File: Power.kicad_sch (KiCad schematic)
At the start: 30 parts, among them J1 1769, U6 EA3036C, U9 BQ24074RGTR

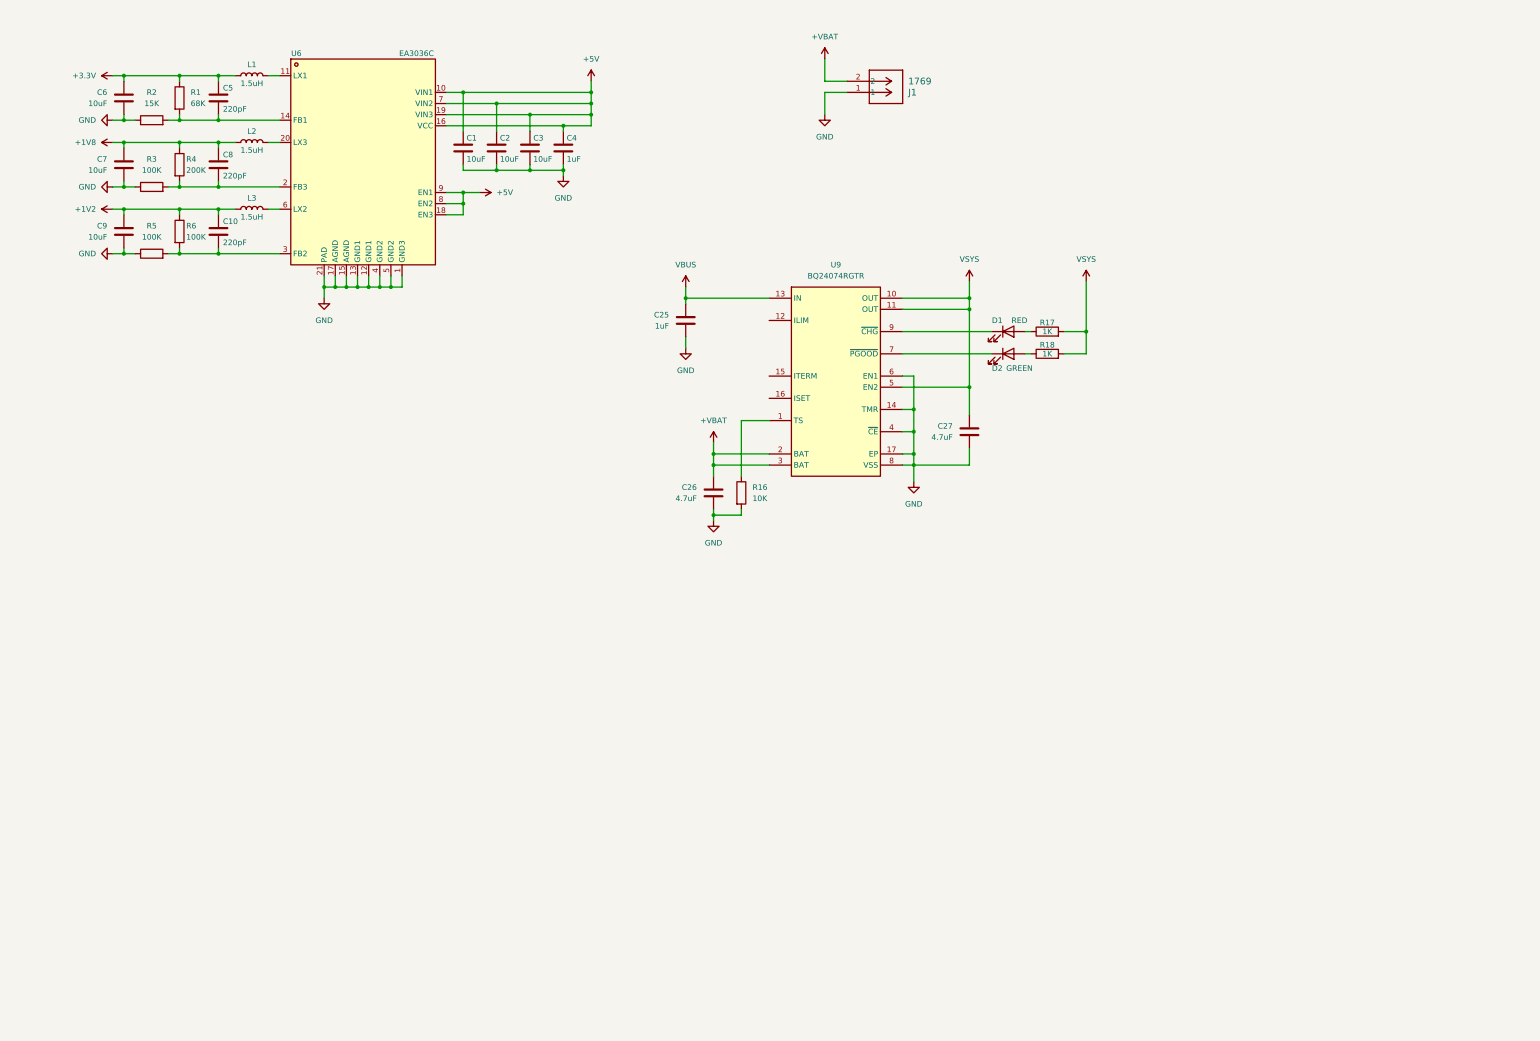
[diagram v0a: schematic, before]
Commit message: power changes, audio changes, testing layout
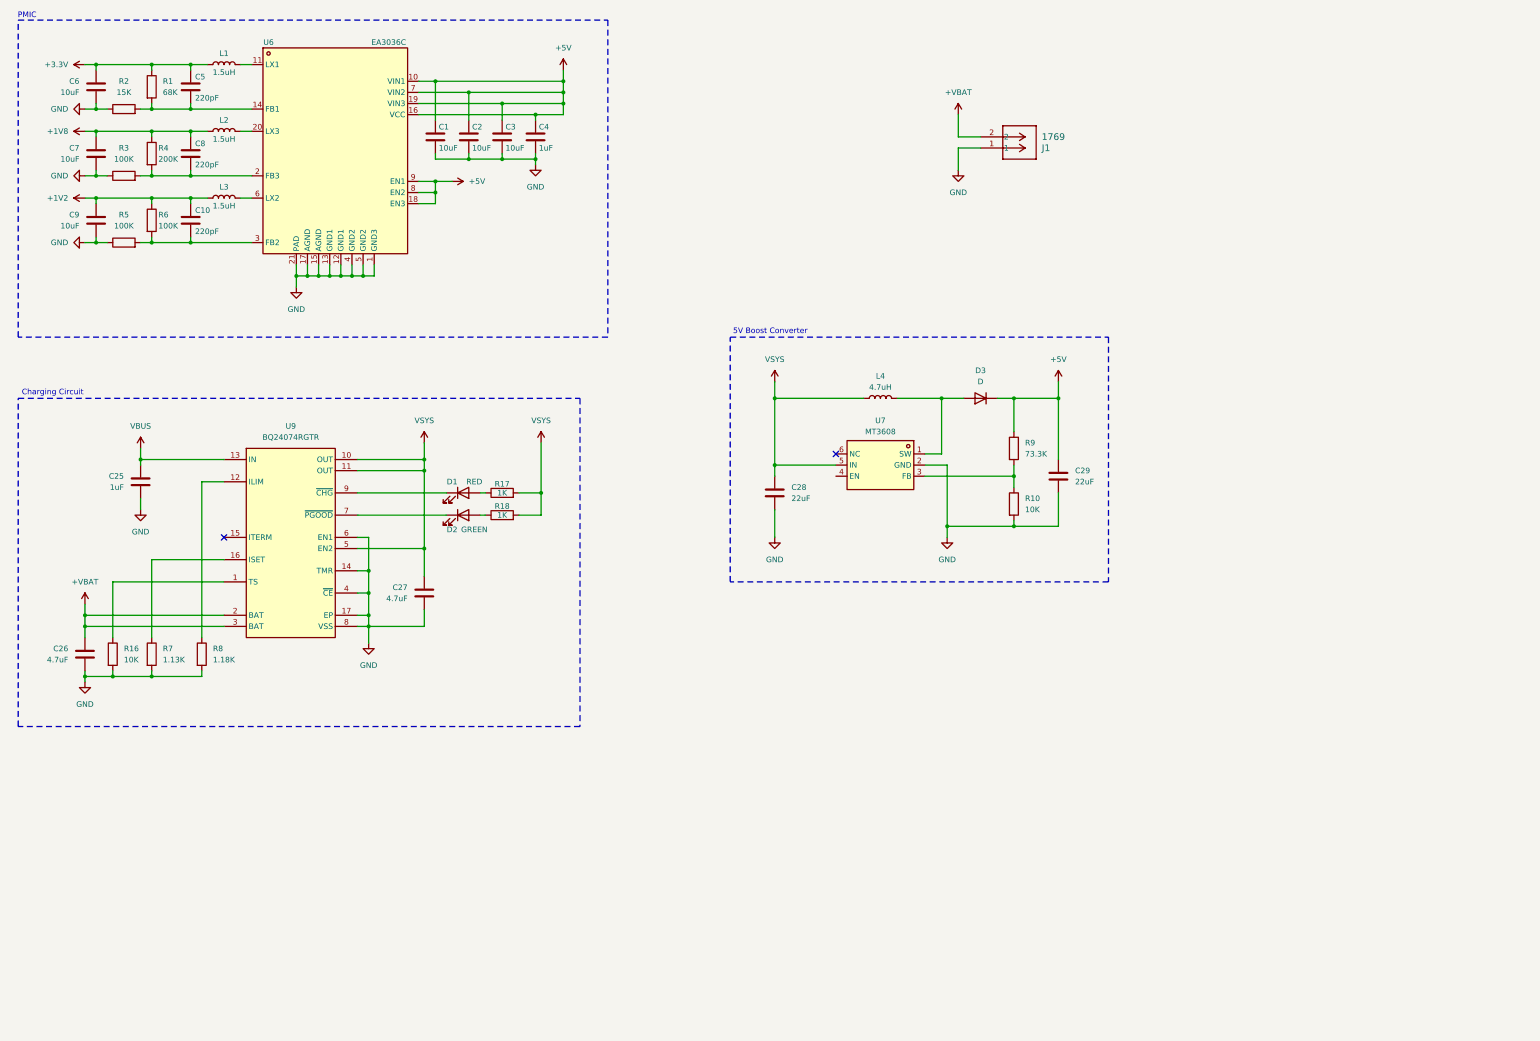
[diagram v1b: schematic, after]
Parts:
- added C28, C29: 22uF, symbol Device:C
- added D3: D, symbol Device:D
- added L4: 4.7uH, symbol Device:L
- added R10: 10K, symbol Device:R
- added R7: 1.13K, symbol Device:R
- added R8: 1.18K, symbol Device:R
- added R9: 73.3K, symbol Device:R
- added U7: MT3608, easyeda2kicad:SOT-23-6_L2.9-W1.6-P0.95-LS2.8-BL, symbol easyeda2kicad:MT3608
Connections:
- net +5V: now also C29.1, D3.1 (K), R9.1
- net GND: now also C28.2, C29.2, R10.2, R7.2, R8.2, U7.2 (GND)
- net VSYS: now also C28.1, L4.1, U7.5 (IN)
- net at U9.12 (ILIM): now also R8.1
- net at U9.16 (ISET): now also R7.1
- new net: D3.2 (A), L4.2, U7.1 (SW)
- new net: R10.1, R9.2, U7.3 (FB)
- no-connect marks 0 -> 2
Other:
- note added: "5V Boost Converter"
- note added: "Charging Circuit"
- note added: "PMIC"
- moved on the sheet: C1, C10, C2, C25, C26, C27, C3, C4, C5, C6, C7, C8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

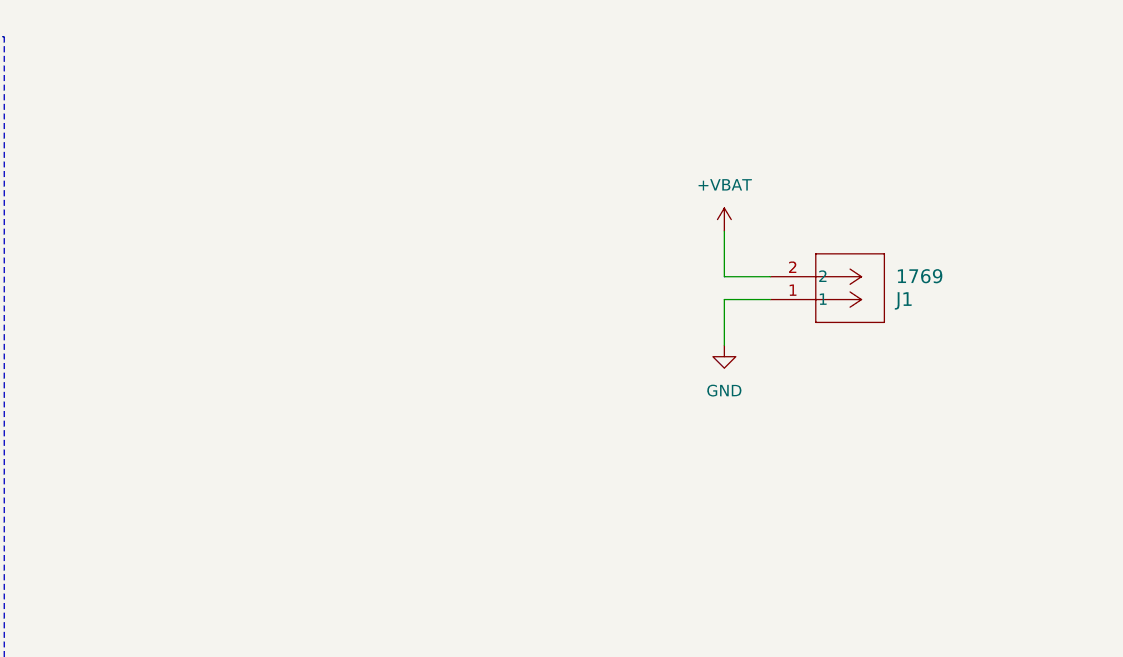
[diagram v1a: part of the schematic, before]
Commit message: power changes to v3s, nand
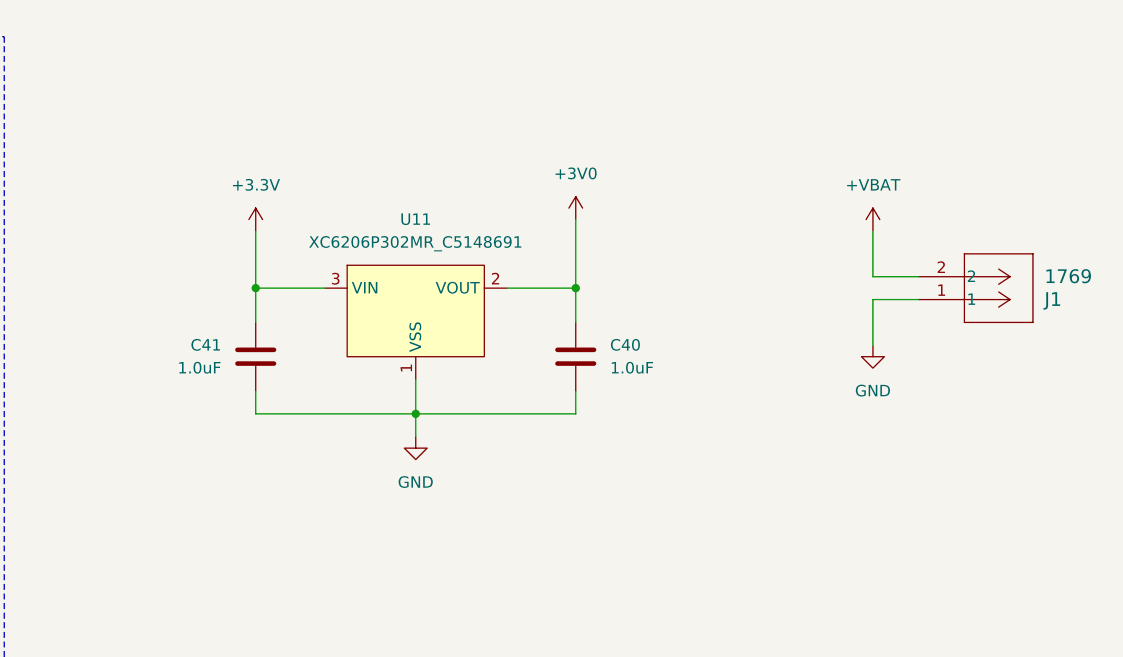
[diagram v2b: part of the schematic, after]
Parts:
- added C40, C41: 1.0uF, symbol Device:C
- added U11: XC6206P302MR_C5148691, easyeda2kicad:SOT-23-3_L3.0-W1.7-P0.95-LS2.9-BR, symbol easyeda2kicad:XC6206P302MR_C5148691
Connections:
- net +3.3V: now also C41.1, U11.3 (VIN)
- net GND: now also C40.2, C41.2, U11.1 (VSS)
- new net +3V0: C40.1, U11.2 (VOUT)
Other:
- moved on the sheet: J1

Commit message: power changes for v3s, cleanup
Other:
- note added: "3.0V LDO"
- title: (none) -> iPodClone
- moved on the sheet: C28, C29, C40, C41, D3, J1, L4, R10, R9, U11, U7

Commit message: gitignore and audio changes
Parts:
- added C50: 2.2uF, symbol Device:C
- added C51: 1uF, symbol Device:C
- added R30, R31: 10K, symbol Device:R
- added R33: 10M, symbol Device:R
- added U4: BQ27220YZFR, easyeda2kicad:DSBGA-9_L1.7-W1.6-R3-C3-P0.50-BL, symbol easyeda2kicad:BQ27220YZFR
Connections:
- net +3.3V: now also R31.1, R33.1, U4.C2 (SRN)
- net +VBAT: now also C51.1, R33.2, U4.C1 (SRP), U4.C3 (BAT)
- net GND: now also C50.2, C51.2, R30.2, U4.B2 (VSS)
- new net: R30.1, U4.B1 (BIN)
- new net: C50.1, U4.B3 (VDD)
- new net GPOUT: R31.2, U4.A1 (GPOUT)
- new net I2C_SCK: U4.A3 (SCL)
- new net I2C_SDA: U4.A2 (SDA)
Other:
- note added: "Battery fuel gauge"
- moved on the sheet: C1, C10, C2, C25, C26, C27, C28, C29, C3, C4, C40, C41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
